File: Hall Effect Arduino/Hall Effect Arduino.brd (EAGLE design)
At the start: 100 x 80 mm, 23 parts, among them U1 ATMEGA328P, U2 M5205 5v, X1 Power In, Y1 16MHz

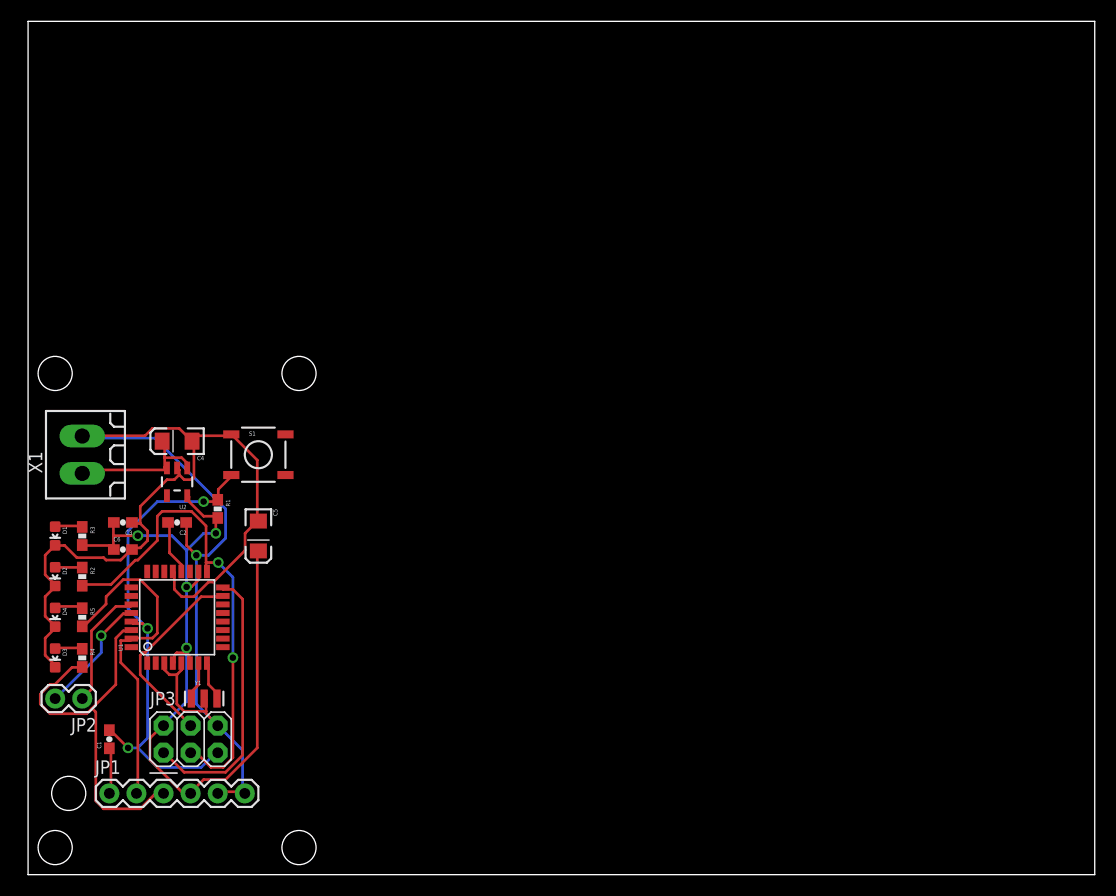
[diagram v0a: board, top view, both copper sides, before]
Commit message: Updated with header pins
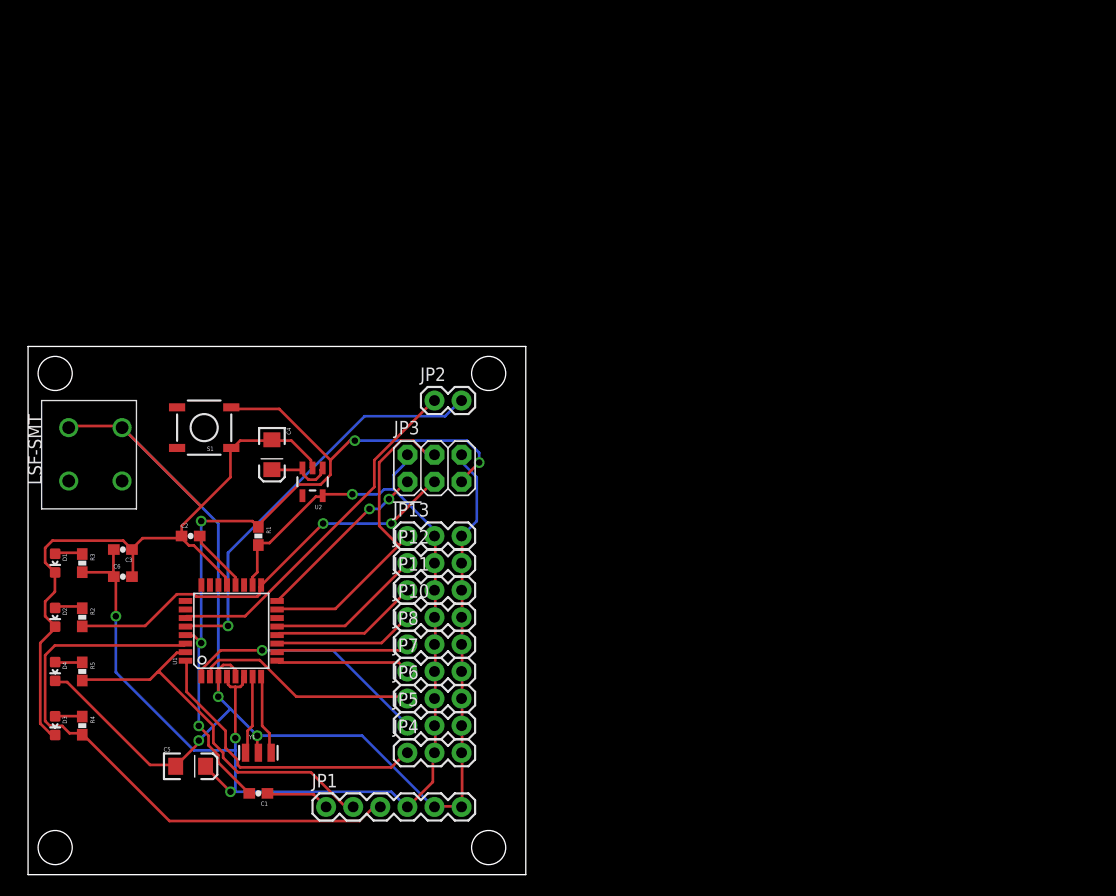
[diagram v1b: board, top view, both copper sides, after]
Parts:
- removed X1: Power In, con-weidmueller-sl35:180G-2
- added JP10, JP11, JP12, JP13, JP4, JP5, JP6, JP7, JP8: (no value), SparkFun-Connectors:1X03
- added U$1: LSF-SMT, LSF-SMT:LSF-SMT
- moved JP2 43.3 mm to (38.1, 44.5), turned to 0 degrees
- moved JP3 34.2 mm to (38.1, 38.1)
- moved C5 22.5 mm to (15.2, 10.2), turned to 0 degrees
- moved JP1 20.4 mm to (27.9, 6.35)
- moved C1 14.9 mm to (21.6, 7.62), turned to 180 degrees
- moved U2 12.7 mm to (26.7, 36.8)
- moved C4 8.98 mm to (22.9, 39.4), turned to 270 degrees
- moved Y1 7.18 mm to (21.6, 11.4)
- moved D3 6.35 mm to (2.54, 14.0)
- moved R4 6.35 mm to (5.08, 14.0)
- moved S1 5.68 mm to (16.5, 41.9), turned to 180 degrees
- moved U1 5.24 mm to (19.1, 22.9)
- moved D4 5.08 mm to (2.54, 19.1)
- moved R5 5.08 mm to (5.08, 19.1)
- moved R1 4.58 mm to (21.6, 31.8)
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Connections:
- net D2: now also JP4.1
- net D3: now also JP5.1
- net D4: now also JP6.1
- net D5: now also JP7.1
- net D6: now also JP8.1
- net D7: now also JP10.1
- net D8: now also JP11.1
- net D9: now also JP12.1
- net GND: now also JP10.3, JP11.3, JP12.3, JP13.3, JP4.3, JP5.3, JP6.3, JP7.3, JP8.3, U$1.1, U$1.1-2; no longer X1.2
- net MOSI: now also JP13.1
- net VCC: now also JP10.2, JP11.2, JP12.2, JP13.2, JP4.2, JP5.2, JP6.2, JP7.2, JP8.2
- net VIN: no longer X1.1
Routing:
- net GND: track 141.7 -> 198.1 mm, vias 1 -> 3
- net VCC: track 80.8 -> 118.5 mm
- net D2: track 0.00 -> 28.4 mm
- net SCL: track 11.4 -> 38.7 mm
- net RESET: track 47.9 -> 75.1 mm, vias 3 -> 5
- net D3: track 0.00 -> 23.7 mm, vias 0 -> 1
- net SDA: track 11.5 -> 33.3 mm
- net D4: track 0.00 -> 21.1 mm
- net RXI: track 36.7 -> 55.7 mm
- net D9: track 0.00 -> 14.7 mm
- net D8: track 0.00 -> 14.0 mm
- net D7: track 0.00 -> 13.2 mm
- net D5: track 0.00 -> 12.6 mm
- net D6: track 0.00 -> 12.5 mm
- net MOSI: track 18.6 -> 30.2 mm
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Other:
- board size 100 x 80 mm -> 46.7 x 49.5 mm

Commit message: Updated with final board for production.
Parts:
- removed JP10, JP11, JP12, JP13, JP4, JP5, JP6, JP7, JP8: (no value), SparkFun-Connectors:1X03
- removed JP2: I2C, SparkFun-Connectors:1X02
- added 10, 2, 3, 4, 5, 6, 7, 8, 9, I2C: (no value), SparkFun-Connectors:1X03
- moved C1 15.3 mm to (11.4, 19.1), turned to 90 degrees
- moved Y1 14.5 mm to (33.0, 2.54)
- moved JP1 11.4 mm to (16.5, 6.35), turned to 180 degrees
- moved C5 10.8 mm to (22.9, 2.54)
- moved C4 9.16 mm to (30.5, 44.5), turned to 180 degrees
- moved U1 7.41 mm to (22.9, 16.5)
- moved D3 6.35 mm to (2.54, 20.3)
- moved R4 6.35 mm to (5.08, 20.3)
- moved JP3 5.68 mm to (40.6, 33.0)
- moved D4 5.08 mm to (2.54, 24.1)
- moved R5 5.08 mm to (5.08, 24.1)
- moved D2 3.81 mm to (2.54, 27.9)
- moved R2 3.81 mm to (5.08, 27.9)
- moved U2 3.81 mm to (30.5, 36.8)
- moved C2 3.59 mm to (17.8, 34.3), turned to 180 degrees
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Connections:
- net D10: now also 10.1
- net D2: now also 2.1; no longer JP4.1
- net D3: now also 3.1; no longer JP5.1
- net D4: now also 4.1; no longer JP6.1
- net D5: now also 5.1; no longer JP7.1
- net D6: now also 6.1; no longer JP8.1
- net D7: now also 7.1; no longer JP10.1
- net D8: now also 8.1; no longer JP11.1
- net D9: now also 9.1; no longer JP12.1
- net GND: now also 10.3, 2.3, 3.3, 4.3, 5.3, 6.3, 7.3, 8.3, 9.3, I2C.3; no longer JP10.3, JP11.3, JP12.3, JP13.3, JP4.3, JP5.3, JP6.3, JP7.3, JP8.3
- net MOSI: no longer JP13.1
- net SCL: now also I2C.2; no longer JP2.2
- net SDA: now also I2C.1; no longer JP2.1
- net VCC: now also 10.2, 2.2, 3.2, 4.2, 5.2, 6.2, 7.2, 8.2, 9.2; no longer JP10.2, JP11.2, JP12.2, JP13.2, JP4.2, JP5.2, JP6.2, JP7.2, JP8.2
- net VIN: now also U$1.2, U$1.2-2
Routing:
- net VIN: track 6.35 -> 49.9 mm, vias 0 -> 2
- net VCC: track 118.5 -> 153.0 mm, vias 4 -> 0
- net N$2: track 7.64 -> 38.2 mm, vias 0 -> 2
- net SCL: track 38.7 -> 14.5 mm
- net RXI: track 55.7 -> 34.2 mm, vias 0 -> 1
- net DTR: track 6.01 -> 25.2 mm
- net SDA: track 33.3 -> 14.8 mm
- net AREF: track 5.97 -> 23.6 mm, vias 0 -> 2
- net GND: track 198.1 -> 181.1 mm, vias 3 -> 0
- net D10: track 0.00 -> 15.3 mm
- net SCK: track 39.2 -> 47.9 mm
- net N$1: track 7.51 -> 14.4 mm, vias 0 -> 2
- net RESET: track 75.1 -> 81.4 mm, vias 5 -> 2
- net D4: track 21.1 -> 26.1 mm, vias 0 -> 3
- net TXO: track 35.5 -> 40.1 mm
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- added copper zone on layer 16, net GND
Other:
- board text added: "+"
- board text added: "+5"
- board text added: "-"
- board text added: "G"
- board text added: "GND"
- board text added: "Reset"
- board text added: "SCL"
- board text added: "SDA"
- board text added: "Sig"
- board text added: "WildStang Arduino breakout v1.0 2 Feb 2015"
